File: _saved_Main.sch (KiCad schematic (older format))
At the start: 70 parts, among them J6 Conn_01x03, J7 Conn_01x03, J8 Conn_01x06, Q1 CSD17307Q5A, Q2 CSD17307Q5A, U1 LM4120AIM5-5.0, U2 LTC2942, U3 LM393, U4 TPS2557, U5 LM393, U6 TPS2557, U7 SN74LVC2G08

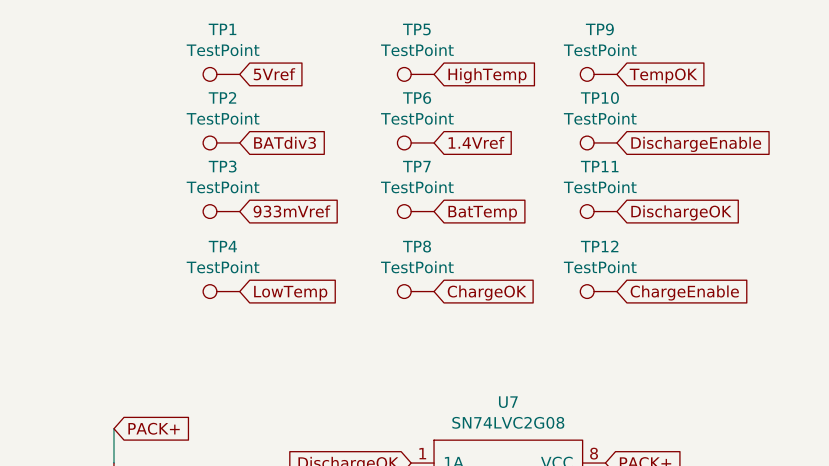
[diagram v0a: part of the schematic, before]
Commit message: Added footprints for symbols, need to find schottkys
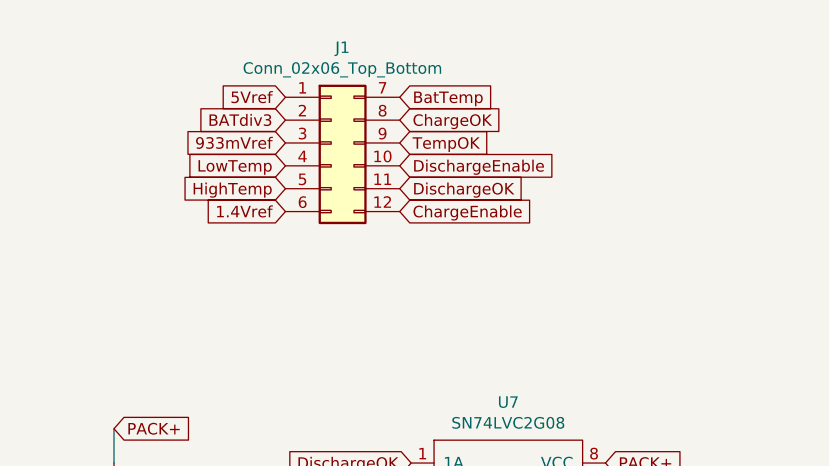
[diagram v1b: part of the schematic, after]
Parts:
- removed TP1, TP10, TP11, TP12, TP2, TP3, TP4, TP5, TP6, TP7, TP8, TP9: TestPoint, symbol Connector:TestPoint
- added J1: Conn_02x06_Top_Bottom, Connector_PinHeader_2.00mm:PinHeader_2x06_P2.00mm_Vertical, symbol Connector_Generic:Conn_02x06_Top_Bottom
- AL/CC1, BAT+1, BAT-1, PACK+1, SCL1, SDA1: footprint (none) -> Connector_PinHeader_2.00mm:PinHeader_1x01_P2.00mm_Vertical
- C1, C4, C5, C6, C7, C8: footprint (none) -> Capacitor_SMD:C_1206_3216Metric_Pad1.42x1.75mm_HandSolder
- C2, C3: footprint Capacitor_SMD:C_1206_3216Metric -> Capacitor_SMD:C_1206_3216Metric_Pad1.42x1.75mm_HandSolder
- R1, R10, R11, R12, R13, R14, R15, R17, R18, R19, R2, R20, R21, R22, R23, R6, R8, R9: footprint (none) -> Resistor_SMD:R_1206_3216Metric_Pad1.42x1.75mm_HandSolder
- R16, R3, R4, R5, R7: footprint Resistor_SMD:R_1206_3216Metric -> Resistor_SMD:R_1206_3216Metric_Pad1.42x1.75mm_HandSolder
- U1: footprint (none) -> Package_TO_SOT_SMD:SOT-23-5_HandSoldering
- U2: footprint (none) -> Package_DFN_QFN:DFN-6-1EP_3x2mm_P0.5mm_EP1.65x1.35mm
- U3, U5: footprint (none) -> Package_SO:SOIC-8-1EP_3.9x4.9mm_P1.27mm_EP2.29x3mm
- U4, U6: footprint (none) -> tps2557:TPS2557
- U7: footprint (none) -> Package_SO:SSOP-8_2.95x2.8mm_P0.65mm
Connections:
- net 1.4Vref: now also J1.6 (Pin_6)
- net 5Vref: now also J1.1 (Pin_1)
- net 933mVref: now also J1.3 (Pin_3)
- net BATdiv3: now also J1.2 (Pin_2)
- net BatTemp: now also J1.7 (Pin_7)
- net ChargeEnable: now also J1.12 (Pin_12)
- net ChargeOK: now also J1.8 (Pin_8)
- net DischargeEnable: now also J1.10 (Pin_10)
- net DischargeOK: now also J1.11 (Pin_11)
- net HighTemp: now also J1.5 (Pin_5)
- net LowTemp: now also J1.4 (Pin_4)
- net TempOK: now also J1.9 (Pin_9)
